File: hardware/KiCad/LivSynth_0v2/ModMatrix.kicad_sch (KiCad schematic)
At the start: 7 parts, among them SW3 SW_SPDT, SW4 SW_SPDT

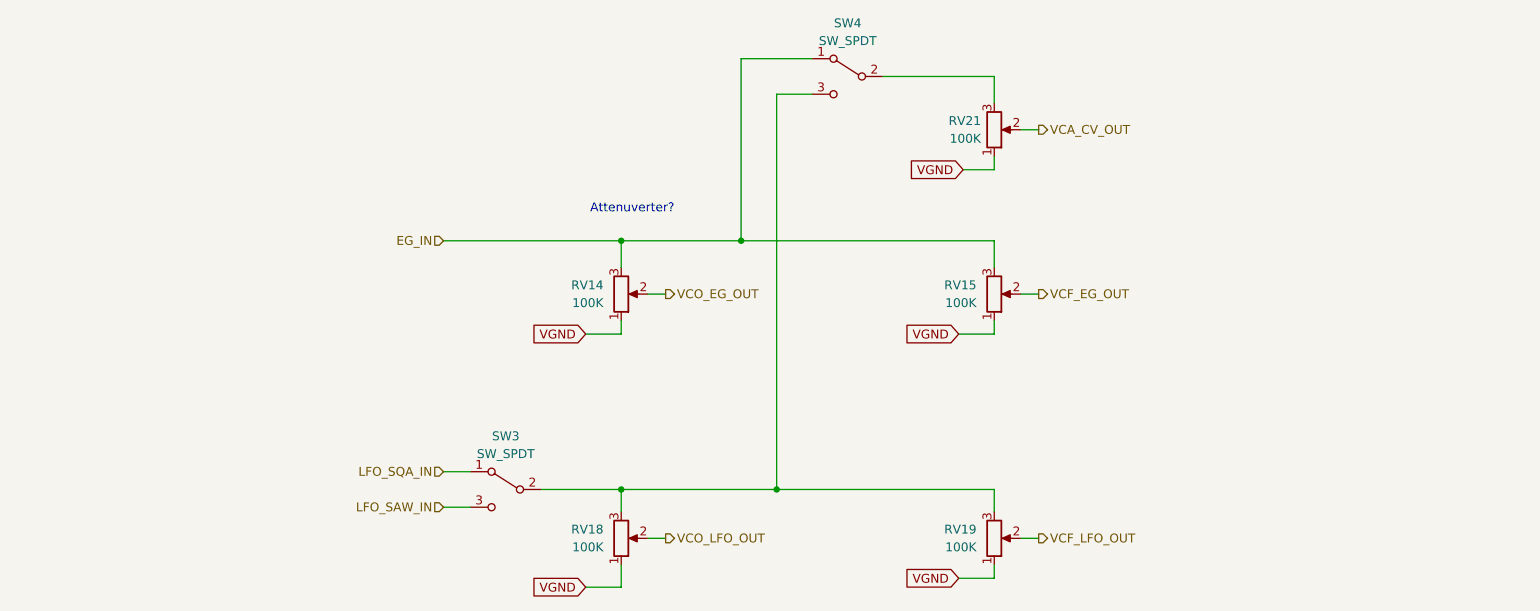
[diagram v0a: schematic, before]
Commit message: Analog redesign:  - Power: Add voltage and current test points  - MCU: use PA11/PA12 for USB DFU interface  - MCU: add NRST reset switch  - Slew: increase portamento cap  - VCO: invert trim pots  - VCF: let resonance kick in earlier  - VCF: invert pots  - VCA: invert trim pot  - EG: full redesign, properly referencing VGND now  - LFO: R61 = 51K  - ModMatrix: add EG attenuverters  - IO: invert pots  - IO: limit output gain for 1W speaker  - IO: connect BTN_SHIFT in gap free order to SR
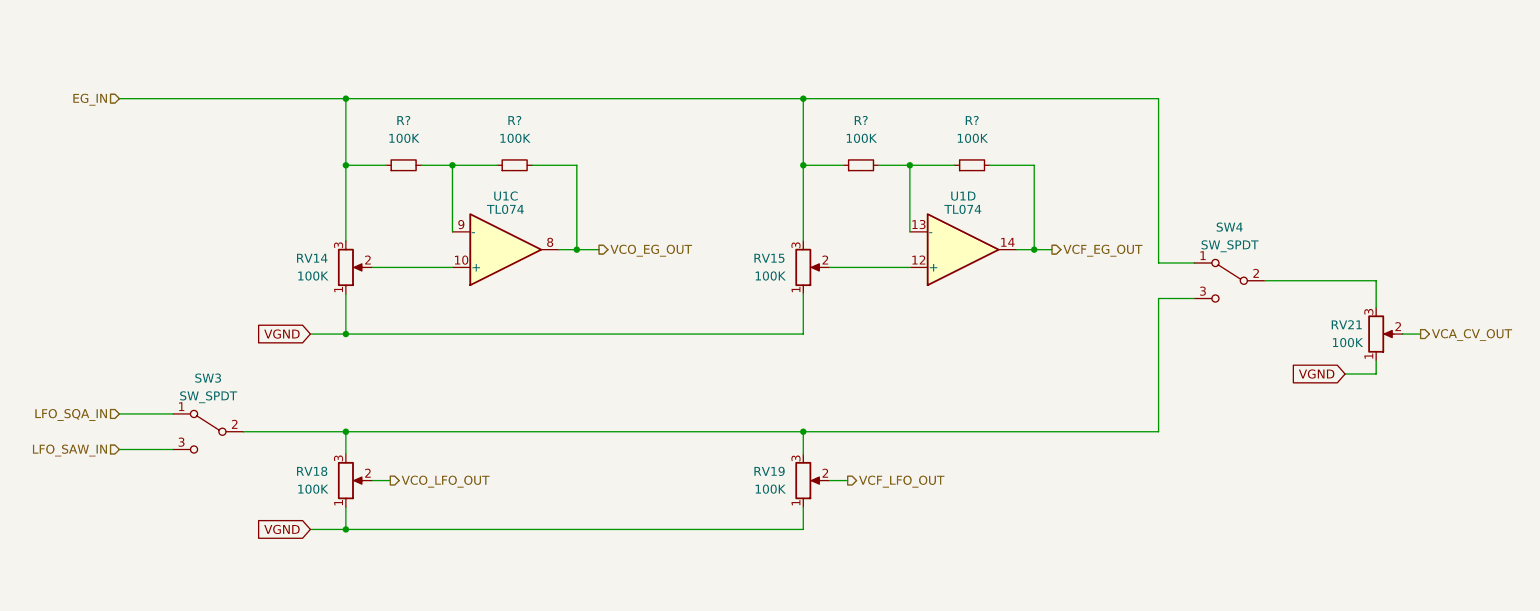
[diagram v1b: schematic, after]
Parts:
- added R? (x4): 100K, symbol Device:R_Small
- added U1: TL074, Package_SO:SOIC-14_3.9x8.7mm_P1.27mm, symbol Amplifier_Operational:TL074
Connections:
- net EG_IN: now also R?.1, R?.1
- net VCF_EG_OUT: now also R?.2, U1.14; no longer RV15.2
- net VCO_EG_OUT: now also R?.2, U1.8; no longer RV14.2
- new net: RV15.2, U1.12 (+)
- new net: R?.1, R?.2, U1.13 (-)
- new net: RV14.2, U1.10 (+)
- new net: R?.1, R?.2, U1.9 (-)
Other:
- note removed: "Attenuverter?"
- moved on the sheet: RV14, RV15, RV18, RV19, RV21, SW3, SW4

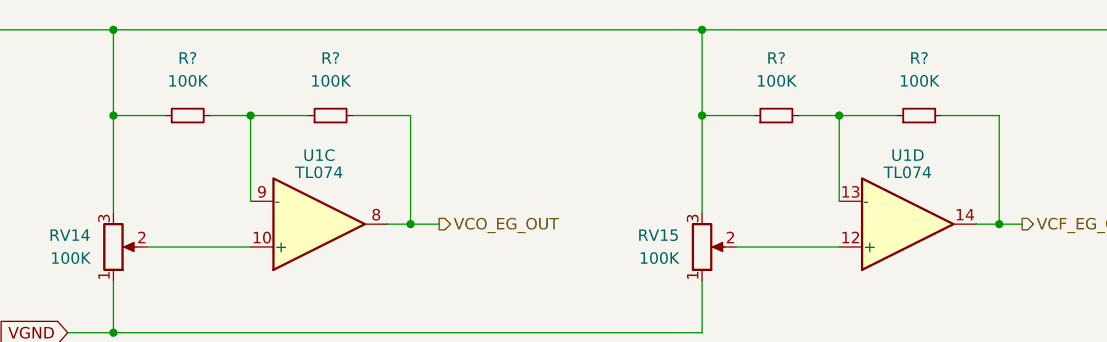
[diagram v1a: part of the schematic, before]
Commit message: Analog Redesign:  - Power: Build ververse polarity protection using P-Mosfet and Zener Diode      - (https://www.youtube.com/watch?v=Ltx4vovY5Z4 - 1:28)  - Power: Build adjustable buck regulator for 8-9V stable voltage source  - PCB: Add location for order number ("JLCJLCJLCJLC")  - General: Add Tooling Holes for PCB assembly  - PCB: check frontend component layout for symmetry  - VCF: fix sound issues  - PCB: Add SloBlo icon  - PCB: Add switch labels to front side  - EG: test new design  - MCU: Add some debug pins
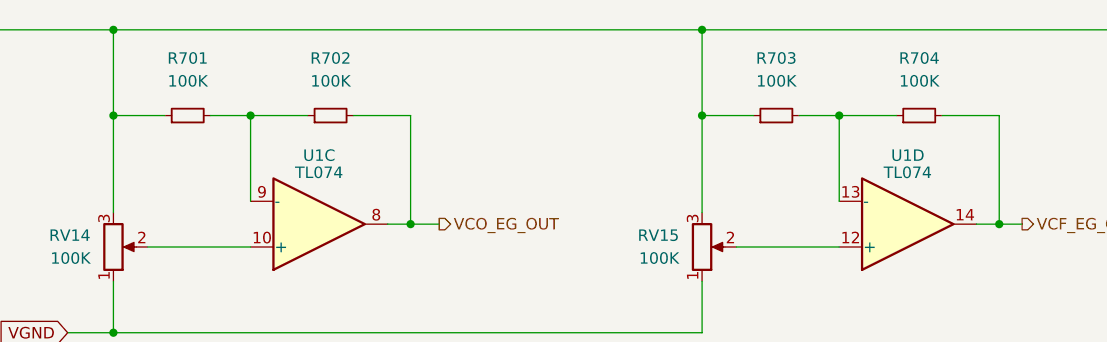
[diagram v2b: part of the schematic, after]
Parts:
- U1: LCSC (none) -> C2057504
- gave numbers to parts that had none: 4
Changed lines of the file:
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@@
   (symbol (lib_id "Device:R_Small") (at 180.975 80.01 90) (unit 1)
     (in_bom yes) (on_board yes) (fields_autoplaced)
-    (property "Reference" "R?" (id 0) (at 180.975 73.66 90))
+    (property "Reference" "R704" (id 0) (at 180.975 73.66 90))
     (property "Value" "100K" (id 1) (at 180.975 76.2 90))
     (property "Footprint" "" (id 2) (at 180.975 80.01 0)
@@
   (symbol (lib_id "Device:R_Small") (at 165.1 80.01 90) (unit 1)
     (in_bom yes) (on_board yes) (fields_autoplaced)
-    (property "Reference" "R?" (id 0) (at 165.1 73.66 90))
+    (property "Reference" "R703" (id 0) (at 165.1 73.66 90))
     (property "Value" "100K" (id 1) (at 165.1 76.2 90))
     (property "Footprint" "" (id 2) (at 165.1 80.01 0)
@@
   (symbol (lib_id "Device:R_Small") (at 115.57 80.01 90) (unit 1)
     (in_bom yes) (on_board yes) (fields_autoplaced)
-    (property "Reference" "R?" (id 0) (at 115.57 73.66 90))
+    (property "Reference" "R702" (id 0) (at 115.57 73.66 90))
     (property "Value" "100K" (id 1) (at 115.57 76.2 90))
     (property "Footprint" "" (id 2) (at 115.57 80.01 0)
@@
   (symbol (lib_id "Device:R_Small") (at 99.695 80.01 90) (unit 1)
     (in_bom yes) (on_board yes) (fields_autoplaced)
-    (property "Reference" "R?" (id 0) (at 99.695 73.66 90))
+    (property "Reference" "R701" (id 0) (at 99.695 73.66 90))
     (property "Value" "100K" (id 1) (at 99.695 76.2 90))
     (property "Footprint" "" (id 2) (at 99.695 80.01 0)
@@
     )
     (property "Datasheet" "http://www.ti.com/lit/ds/symlink/tl071.pdf" (id 3) (at 180.975 97.155 0)
+      (effects (font (size 1.27 1.27)) hide)
+    )
+    (property "LCSC" "C2057504" (id 4) (at 179.705 92.075 0)
       (effects (font (size 1.27 1.27)) hide)
     )
@@
       (effects (font (size 1.27 1.27)) hide)
     )
+    (property "LCSC" "C2057504" (id 4) (at 114.3 92.075 0)
+      (effects (font (size 1.27 1.27)) hide)
+    )

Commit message: progress 2023-01-21
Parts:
- R701, R702, R703, R704: footprint (none) -> Resistor_THT:R_Axial_DIN0207_L6.3mm_D2.5mm_P7.62mm_Horizontal
- renumbered U1 to U3
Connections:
- net VCF_EG_OUT: now also U3.1; no longer U3.14
- net VCO_EG_OUT: now also U3.7; no longer U3.8
- net at RV15.2: now also U3.3 (+); no longer U3.12 (+)
- net at R703.2, R704.1: now also U3.2 (-); no longer U3.13 (-)
- net at RV14.2: now also U3.5 (+); no longer U3.10 (+)
- net at R701.2, R702.1: now also U3.6 (-); no longer U3.9 (-)
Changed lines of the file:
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@@
     (property "Reference" "R704" (id 0) (at 180.975 73.66 90))
     (property "Value" "100K" (id 1) (at 180.975 76.2 90))
-    (property "Footprint" "" (id 2) (at 180.975 80.01 0)
+    (property "Footprint" "Resistor_THT:R_Axial_DIN0207_L6.3mm_D2.5mm_P7.62mm_Horizontal" (id 2) (at 180.975 80.01 0)
       (effects (font (size 1.27 1.27)) hide)
     )
@@
     (property "Reference" "R703" (id 0) (at 165.1 73.66 90))
     (property "Value" "100K" (id 1) (at 165.1 76.2 90))
-    (property "Footprint" "" (id 2) (at 165.1 80.01 0)
+    (property "Footprint" "Resistor_THT:R_Axial_DIN0207_L6.3mm_D2.5mm_P7.62mm_Horizontal" (id 2) (at 165.1 80.01 0)
       (effects (font (size 1.27 1.27)) hide)
     )
@@
     (property "Reference" "R702" (id 0) (at 115.57 73.66 90))
     (property "Value" "100K" (id 1) (at 115.57 76.2 90))
-    (property "Footprint" "" (id 2) (at 115.57 80.01 0)
+    (property "Footprint" "Resistor_THT:R_Axial_DIN0207_L6.3mm_D2.5mm_P7.62mm_Horizontal" (id 2) (at 115.57 80.01 0)
       (effects (font (size 1.27 1.27)) hide)
     )
@@
     (property "Reference" "R701" (id 0) (at 99.695 73.66 90))
     (property "Value" "100K" (id 1) (at 99.695 76.2 90))
-    (property "Footprint" "" (id 2) (at 99.695 80.01 0)
+    (property "Footprint" "Resistor_THT:R_Axial_DIN0207_L6.3mm_D2.5mm_P7.62mm_Horizontal" (id 2) (at 99.695 80.01 0)
       (effects (font (size 1.27 1.27)) hide)
     )
@@
     (pin "3")
   )
-  (symbol (lib_id "Amplifier_Operational:TL074") (at 179.705 92.075 0) (mirror x) (unit 4)
+  (symbol (lib_id "Amplifier_Operational:TL074") (at 179.705 92.075 0) (mirror x) (unit 1)
     (in_bom yes) (on_board yes)
-    (property "Reference" "U1" (id 0) (at 179.705 84.455 0))
+    (property "Reference" "U3" (id 0) (at 179.705 84.455 0))
     (property "Value" "TL074" (id 1) (at 179.705 86.36 0))
     (property "Footprint" "Package_SO:SOIC-14_3.9x8.7mm_P1.27mm" (id 2) (at 178.435 94.615 0)
@@
     (pin "3")
   )
-  (symbol (lib_id "Amplifier_Operational:TL074") (at 114.3 92.075 0) (mirror x) (unit 3)
+  (symbol (lib_id "Amplifier_Operational:TL074") (at 114.3 92.075 0) (mirror x) (unit 2)
     (in_bom yes) (on_board yes)
-    (property "Reference" "U1" (id 0) (at 114.3 84.455 0))
+    (property "Reference" "U3" (id 0) (at 114.3 84.455 0))
     (property "Value" "TL074" (id 1) (at 114.3 86.36 0))
     (property "Footprint" "Package_SO:SOIC-14_3.9x8.7mm_P1.27mm" (id 2) (at 113.03 94.615 0)

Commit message: Geographical reannotate
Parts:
- renumbered R704 to R78, R703 to R79, R702 to R80, R701 to R81, RV14 to RV13, RV15 to RV14, RV21 to RV22, U3 to U4
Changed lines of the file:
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@@
   (symbol (lib_id "Device:R_Potentiometer") (at 156.845 94.615 0) (mirror x) (unit 1)
     (in_bom yes) (on_board yes) (fields_autoplaced)
-    (property "Reference" "RV15" (id 0) (at 154.305 93.3449 0)
+    (property "Reference" "RV14" (id 0) (at 154.305 93.3449 0)
       (effects (font (size 1.27 1.27)) (justify right))
     )
@@
   (symbol (lib_id "Device:R_Small") (at 180.975 80.01 90) (unit 1)
     (in_bom yes) (on_board yes) (fields_autoplaced)
-    (property "Reference" "R704" (id 0) (at 180.975 73.66 90))
+    (property "Reference" "R78" (id 0) (at 180.975 73.66 90))
     (property "Value" "100K" (id 1) (at 180.975 76.2 90))
     (property "Footprint" "Resistor_THT:R_Axial_DIN0207_L6.3mm_D2.5mm_P7.62mm_Horizontal" (id 2) (at 180.975 80.01 0)
@@
   (symbol (lib_id "Device:R_Small") (at 165.1 80.01 90) (unit 1)
     (in_bom yes) (on_board yes) (fields_autoplaced)
-    (property "Reference" "R703" (id 0) (at 165.1 73.66 90))
+    (property "Reference" "R79" (id 0) (at 165.1 73.66 90))
     (property "Value" "100K" (id 1) (at 165.1 76.2 90))
     (property "Footprint" "Resistor_THT:R_Axial_DIN0207_L6.3mm_D2.5mm_P7.62mm_Horizontal" (id 2) (at 165.1 80.01 0)
@@
   (symbol (lib_id "Device:R_Potentiometer") (at 91.44 94.615 0) (mirror x) (unit 1)
     (in_bom yes) (on_board yes) (fields_autoplaced)
-    (property "Reference" "RV14" (id 0) (at 88.9 93.3449 0)
+    (property "Reference" "RV13" (id 0) (at 88.9 93.3449 0)
       (effects (font (size 1.27 1.27)) (justify right))
     )
@@
   (symbol (lib_id "Device:R_Small") (at 115.57 80.01 90) (unit 1)
     (in_bom yes) (on_board yes) (fields_autoplaced)
-    (property "Reference" "R702" (id 0) (at 115.57 73.66 90))
+    (property "Reference" "R80" (id 0) (at 115.57 73.66 90))
     (property "Value" "100K" (id 1) (at 115.57 76.2 90))
     (property "Footprint" "Resistor_THT:R_Axial_DIN0207_L6.3mm_D2.5mm_P7.62mm_Horizontal" (id 2) (at 115.57 80.01 0)
@@
   (symbol (lib_id "Device:R_Small") (at 99.695 80.01 90) (unit 1)
     (in_bom yes) (on_board yes) (fields_autoplaced)
-    (property "Reference" "R701" (id 0) (at 99.695 73.66 90))
+    (property "Reference" "R81" (id 0) (at 99.695 73.66 90))
     (property "Value" "100K" (id 1) (at 99.695 76.2 90))
     (property "Footprint" "Resistor_THT:R_Axial_DIN0207_L6.3mm_D2.5mm_P7.62mm_Horizontal" (id 2) (at 99.695 80.01 0)
@@
   (symbol (lib_id "Device:R_Potentiometer") (at 238.76 104.14 0) (mirror x) (unit 1)
     (in_bom yes) (on_board yes) (fields_autoplaced)
-    (property "Reference" "RV21" (id 0) (at 236.855 102.8699 0)
+    (property "Reference" "RV22" (id 0) (at 236.855 102.8699 0)
       (effects (font (size 1.27 1.27)) (justify right))
     )
@@
   (symbol (lib_id "Amplifier_Operational:TL074") (at 179.705 92.075 0) (mirror x) (unit 1)
     (in_bom yes) (on_board yes)
-    (property "Reference" "U3" (id 0) (at 179.705 84.455 0))
+    (property "Reference" "U4" (id 0) (at 179.705 84.455 0))
     (property "Value" "TL074" (id 1) (at 179.705 86.36 0))
     (property "Footprint" "Package_SO:SOIC-14_3.9x8.7mm_P1.27mm" (id 2) (at 178.435 94.615 0)
@@
   (symbol (lib_id "Amplifier_Operational:TL074") (at 114.3 92.075 0) (mirror x) (unit 2)
     (in_bom yes) (on_board yes)
-    (property "Reference" "U3" (id 0) (at 114.3 84.455 0))
+    (property "Reference" "U4" (id 0) (at 114.3 84.455 0))
     (property "Value" "TL074" (id 1) (at 114.3 86.36 0))
     (property "Footprint" "Package_SO:SOIC-14_3.9x8.7mm_P1.27mm" (id 2) (at 113.03 94.615 0)

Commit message: Modify toggle switches (footprint and 3D model) Align R value designators Add JLC component placement checkup file
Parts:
- SW3, SW4: footprint SloBlo:SW_Toggle_MS500C -> SloBlo:SW_Toggle_MS500
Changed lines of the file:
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@@
     (property "Reference" "SW4" (id 0) (at 217.805 88.9 0))
     (property "Value" "SW_SPDT" (id 1) (at 217.805 91.44 0))
-    (property "Footprint" "SloBlo:SW_Toggle_MS500C" (id 2) (at 217.805 96.52 0)
+    (property "Footprint" "SloBlo:SW_Toggle_MS500" (id 2) (at 217.805 96.52 0)
       (effects (font (size 1.27 1.27)) hide)
     )
@@
     (property "Reference" "SW3" (id 0) (at 71.755 110.49 0))
     (property "Value" "SW_SPDT" (id 1) (at 71.755 113.03 0))
-    (property "Footprint" "SloBlo:SW_Toggle_MS500C" (id 2) (at 71.755 118.11 0)
+    (property "Footprint" "SloBlo:SW_Toggle_MS500" (id 2) (at 71.755 118.11 0)
       (effects (font (size 1.27 1.27)) hide)
     )

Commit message: Create new 0v3 folder
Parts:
- SW3, SW4: footprint SloBlo:SW_Toggle_MS500 -> SloBlo:SW_Toggle_MS500C
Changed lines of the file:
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@@
     (property "Reference" "SW4" (id 0) (at 217.805 88.9 0))
     (property "Value" "SW_SPDT" (id 1) (at 217.805 91.44 0))
-    (property "Footprint" "SloBlo:SW_Toggle_MS500" (id 2) (at 217.805 96.52 0)
+    (property "Footprint" "SloBlo:SW_Toggle_MS500C" (id 2) (at 217.805 96.52 0)
       (effects (font (size 1.27 1.27)) hide)
     )
@@
     (property "Reference" "SW3" (id 0) (at 71.755 110.49 0))
     (property "Value" "SW_SPDT" (id 1) (at 71.755 113.03 0))
-    (property "Footprint" "SloBlo:SW_Toggle_MS500" (id 2) (at 71.755 118.11 0)
+    (property "Footprint" "SloBlo:SW_Toggle_MS500C" (id 2) (at 71.755 118.11 0)
       (effects (font (size 1.27 1.27)) hide)
     )

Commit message: Reduce EG cap to 4u7 Reduce LFO cap to 220n VCO R23: 470K, C13: 10n
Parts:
- SW3, SW4: footprint SloBlo:SW_Toggle_MS500C -> SloBlo:SW_Toggle_MS500
